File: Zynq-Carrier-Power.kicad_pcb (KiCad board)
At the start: 2 copper layers, 49 x 41 mm, 33 parts, among them J1 Zynq_SoM, J10 Barrel_Jack_MountingPin, J2 B2B-PH-K-S, J3 USB_C_Receptacle_USB2.0_16P, J4 Conn_01x03, J5 Conn_01x03, J6 Conn_01x03, J7 Conn_01x02, J8 Conn_01x02, J9 Conn_01x03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

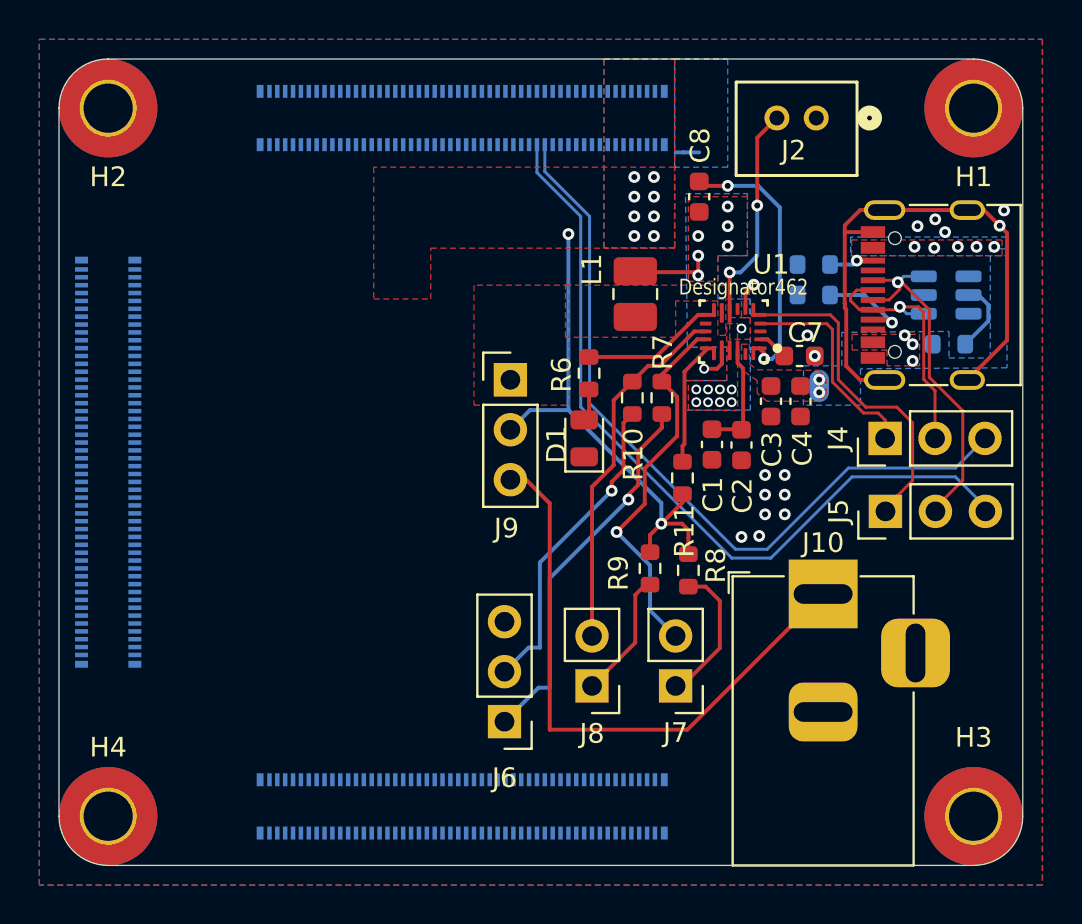
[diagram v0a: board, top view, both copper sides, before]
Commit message: Organized the PCB Layout
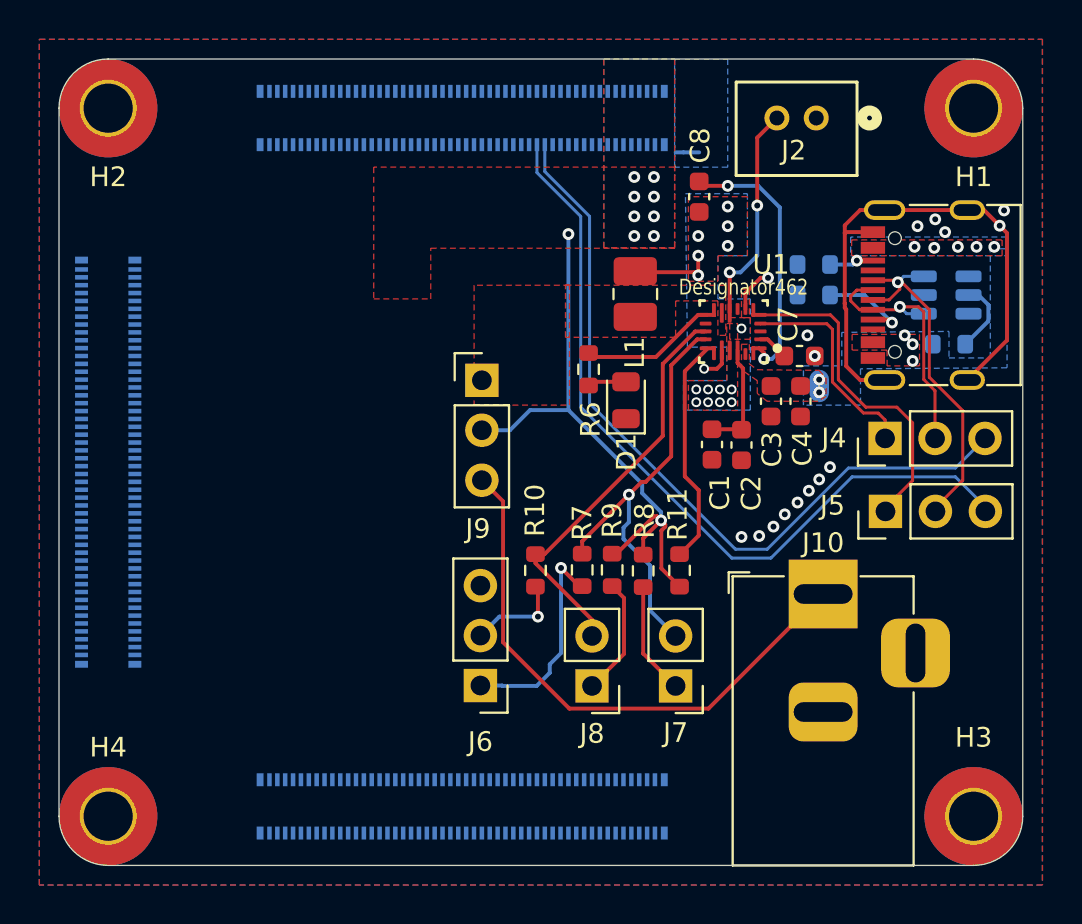
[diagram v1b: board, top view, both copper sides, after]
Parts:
- moved R10 10.1 mm to (121.5, 126.6)
- moved R7 9.64 mm to (123.8, 126.6)
- moved R11 4.70 mm to (128.8, 126.6)
- moved D1 2.88 mm to (126.1, 118.0)
- moved R8 2.30 mm to (126.9, 126.7)
- moved J6 2.21 mm to (118.7, 132.5)
- moved R9 1.93 mm to (125.4, 126.6)
- moved J9 1.45 mm to (118.7, 117.0)
- moved R6 0.20 mm to (124.2, 116.4)
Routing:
- net Net-(J6-Pin_2): track 17.0 -> 4.90 mm
- net Net-(J6-Pin_1): track 19.3 -> 10.8 mm
- net /~{CSn}: track 6.30 -> 11.3 mm
- net +5V: track 27.6 -> 32.1 mm
- net /SCL: track 19.1 -> 22.3 mm
- net /SDA: track 19.1 -> 20.8 mm
- net Net-(J7-Pin_1): track 7.35 -> 5.71 mm
- net Vps: track 30.0 -> 28.8 mm
- net GND: track 31.7 -> 32.6 mm
- net Net-(J8-Pin_1): track 6.50 -> 6.00 mm
